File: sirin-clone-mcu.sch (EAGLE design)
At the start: 3 parts, among them J1 PJ-002A

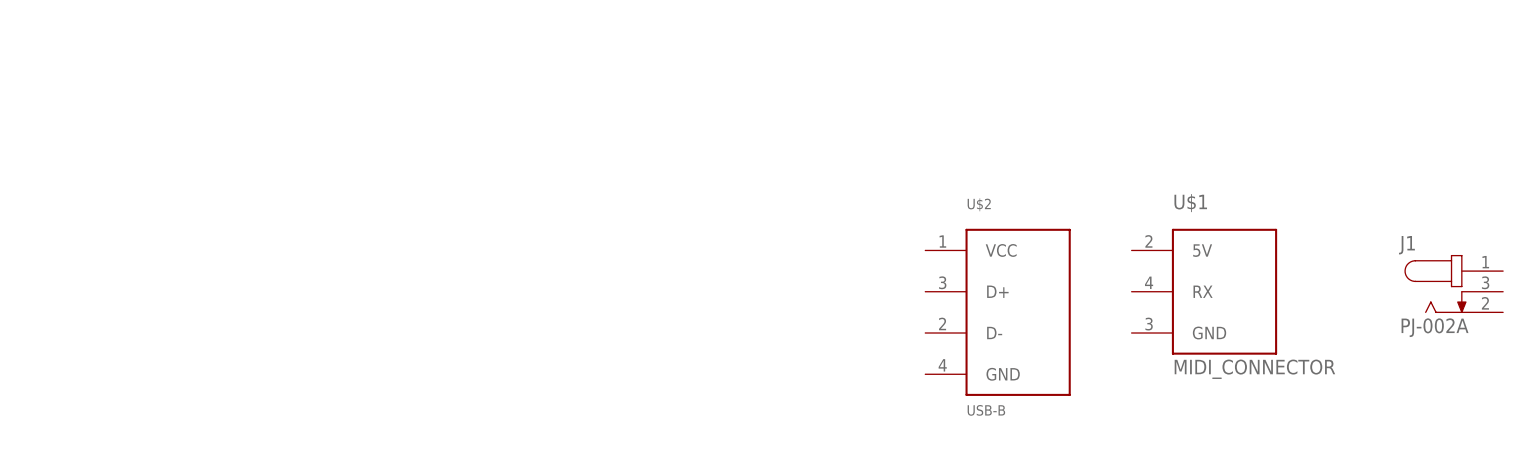
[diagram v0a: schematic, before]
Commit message: add midi
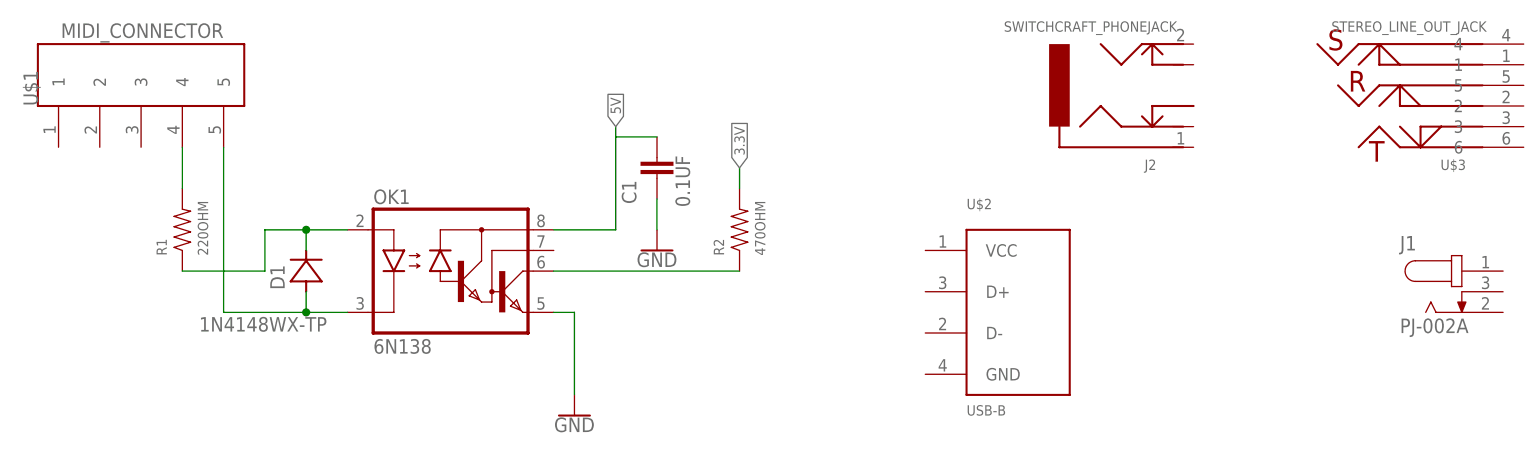
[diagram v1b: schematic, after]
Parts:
- added C1: 0.1UF, sirin-clone-library:0.1UF
- added D1: 1N4148WX-TP, sirin-clone-library:1N4148WX-TP
- added J2: SWITCHCRAFT_PHONEJACK, sirin-clone-library:SWITCHCRAFT_PHONEJACK
- added OK1: 6N138, sirin-clone-library:6N138
- added R1: 220OHM, sirin-clone-library:220OHM
- added R2: 470OHM, sirin-clone-library:470OHM
- added U$3: STEREO_LINE_OUT_JACK, sirin-clone-library:STEREO_LINE_OUT_JACK
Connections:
- new net 3.3V: R2.2
- new net 5V: C1.+, OK1.VCC
- new net GND: C1.-, OK1.GND
- new net N$1: D1.A, OK1.C, U$1.5
- new net N$2: R1.2, U$1.4
- new net N$3: D1.C, OK1.A, R1.1
- new net N$4: OK1.VO, R2.1
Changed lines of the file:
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@@
 </classes>
 <parts>
-<part name="U$1" library="sirin-clone-library" library_urn="urn:adsk.eagle:library:9336050" deviceset="MIDI_CONNECTOR" device="" package3d_urn="urn:adsk.eagle:package:9699785/3"/>
 <part name="J1" library="sirin-clone-library" library_urn="urn:adsk.eagle:library:9336050" deviceset="PJ-002A" device="" package3d_urn="urn:adsk.eagle:package:9702177/2"/>
 <part name="U$2" library="sirin-clone-library" library_urn="urn:adsk.eagle:library:9336050" deviceset="USB-B" device="" package3d_urn="urn:adsk.eagle:package:9702591/4"/>
+<part name="J2" library="sirin-clone-library" library_urn="urn:adsk.eagle:library:9336050" deviceset="SWITCHCRAFT_PHONEJACK" device="" package3d_urn="urn:adsk.eagle:package:8442329/2"/>
+<part name="U$3" library="sirin-clone-library" library_urn="urn:adsk.eagle:library:9336050" deviceset="STEREO_LINE_OUT_JACK" device="" package3d_urn="urn:adsk.eagle:package:9702873/3"/>
+<part name="D1" library="sirin-clone-library" library_urn="urn:adsk.eagle:library:9336050" deviceset="1N4148WX-TP" device="" package3d_urn="urn:adsk.eagle:package:9797239/2"/>
+<part name="R1" library="sirin-clone-library" library_urn="urn:adsk.eagle:library:9336050" deviceset="220OHM" device="" package3d_urn="urn:adsk.eagle:package:8442354/2"/>
+<part name="C1" library="sirin-clone-library" library_urn="urn:adsk.eagle:library:9336050" deviceset="0.1UF" device="" package3d_urn="urn:adsk.eagle:package:8442351/2"/>
+<part name="R2" library="sirin-clone-library" library_urn="urn:adsk.eagle:library:9336050" deviceset="470OHM" device="" package3d_urn="urn:adsk.eagle:package:8442354/2"/>
+<part name="U$1" library="sirin-clone-library" library_urn="urn:adsk.eagle:library:9336050" deviceset="MIDI_CONNECTOR" device="" package3d_urn="urn:adsk.eagle:package:9699785/3"/>
+<part name="OK1" library="sirin-clone-library" library_urn="urn:adsk.eagle:library:9336050" deviceset="6N138" device="" package3d_urn="urn:adsk.eagle:package:9797260/1"/>
+<part name="GND1" library="sirin-clone-library" library_urn="urn:adsk.eagle:library:9336050" deviceset="GND" device=""/>
+<part name="GND2" library="sirin-clone-library" library_urn="urn:adsk.eagle:library:9336050" deviceset="GND" device=""/>
 </parts>
 <sheets>
@@
 </plain>
 <instances>
-<instance part="U$1" gate="G$1" x="20.32" y="38.1" smashed="yes">
-<attribute name="NAME" x="15.24" y="48.26" size="1.778" layer="95"/>
-<attribute name="VALUE" x="15.24" y="27.94" size="1.778" layer="96"/>
-</instance>
 <instance part="J1" gate="G$1" x="50.8" y="38.1" smashed="yes">
 <attribute name="NAME" x="43.17881875" y="43.180790625" size="1.77828125" layer="95"/>
@@
 <attribute name="VALUE" x="-10.16" y="22.86" size="1.27" layer="96"/>
 </instance>
+<instance part="J2" gate="J1" x="10.16" y="63.5" smashed="yes">
+<attribute name="VALUE" x="15.748" y="71.374" size="1.27" layer="96" rot="R180"/>
+<attribute name="NAME" x="13.208" y="54.356" size="1.27" layer="95" rot="R180"/>
+</instance>
+<instance part="U$3" gate="G$1" x="48.26" y="63.5" smashed="yes">
+<attribute name="VALUE" x="53.848" y="71.374" size="1.27" layer="96" rot="R180"/>
+<attribute name="NAME" x="51.308" y="54.356" size="1.27" layer="95" rot="R180"/>
+</instance>
+<instance part="D1" gate="D1" x="-91.44" y="40.64" smashed="yes" rot="R90">
+<attribute name="NAME" x="-94.0816" y="38.3286" size="1.778" layer="95" rot="R90"/>
+<attribute name="VALUE" x="-88.8746" y="34.9758" size="1.778" layer="96" rot="R180"/>
+</instance>
+<instance part="R1" gate="R1" x="-106.68" y="45.72" smashed="yes" rot="R90">
+<attribute name="NAME" x="-108.585" y="42.545" size="1.27" layer="95" rot="R90"/>
+<attribute name="VALUE" x="-103.505" y="42.545" size="1.27" layer="96" rot="R90"/>
+</instance>
+<instance part="C1" gate="C1" x="-48.26" y="53.34" smashed="yes">
+<attribute name="VALUE" x="-44.196" y="48.514" size="1.778" layer="96" font="vector" rot="R90"/>
+<attribute name="NAME" x="-50.8" y="48.895" size="1.778" layer="95" rot="R90"/>
+</instance>
+<instance part="R2" gate="R1" x="-38.1" y="45.72" smashed="yes" rot="R90">
+<attribute name="NAME" x="-40.005" y="42.545" size="1.27" layer="95" rot="R90"/>
+<attribute name="VALUE" x="-34.925" y="42.545" size="1.27" layer="96" rot="R90"/>
+</instance>
+<instance part="U$1" gate="G$1" x="-111.76" y="66.04" smashed="yes" rot="R90">
+<attribute name="NAME" x="-124.46" y="60.96" size="1.778" layer="95" rot="R90"/>
+<attribute name="VALUE" x="-101.6" y="71.12" size="1.778" layer="96" rot="R180"/>
+</instance>
+<instance part="OK1" gate="G$1" x="-73.66" y="40.64" smashed="yes">
+<attribute name="NAME" x="-83.185" y="48.895" size="1.778" layer="95"/>
+<attribute name="VALUE" x="-83.185" y="30.48" size="1.778" layer="96"/>
+</instance>
+<instance part="GND1" gate="1" x="-58.42" y="22.86" smashed="yes">
+<attribute name="VALUE" x="-58.42" y="22.606" size="1.778" layer="96" align="top-center"/>
+</instance>
+<instance part="GND2" gate="1" x="-48.26" y="43.18" smashed="yes">
+<attribute name="VALUE" x="-48.26" y="42.926" size="1.778" layer="96" align="top-center"/>
+</instance>
 </instances>
 <busses>
 </busses>
 <nets>
+<net name="N$1" class="0">
+<segment>
+<pinref part="U$1" gate="G$1" pin="5"/>
+<wire x1="-101.6" y1="55.88" x2="-101.6" y2="35.56" width="0.1524" layer="91"/>
+<pinref part="OK1" gate="G$1" pin="C"/>
+<wire x1="-101.6" y1="35.56" x2="-91.44" y2="35.56" width="0.1524" layer="91"/>
+<pinref part="D1" gate="D1" pin="A"/>
+<wire x1="-91.44" y1="35.56" x2="-86.36" y2="35.56" width="0.1524" layer="91"/>
+<wire x1="-91.44" y1="38.1" x2="-91.44" y2="35.56" width="0.1524" layer="91"/>
+<junction x="-91.44" y="35.56"/>
+</segment>
+</net>
+<net name="N$2" class="0">
+<segment>
+<pinref part="R1" gate="R1" pin="2"/>
+<pinref part="U$1" gate="G$1" pin="4"/>
+<wire x1="-106.68" y1="50.8" x2="-106.68" y2="55.88" width="0.1524" layer="91"/>
+</segment>
+</net>
+<net name="N$3" class="0">
+<segment>
+<pinref part="R1" gate="R1" pin="1"/>
+<wire x1="-106.68" y1="40.64" x2="-96.52" y2="40.64" width="0.1524" layer="91"/>
+<wire x1="-96.52" y1="40.64" x2="-96.52" y2="45.72" width="0.1524" layer="91"/>
+<pinref part="OK1" gate="G$1" pin="A"/>
+<wire x1="-96.52" y1="45.72" x2="-91.44" y2="45.72" width="0.1524" layer="91"/>
+<pinref part="D1" gate="D1" pin="C"/>
+<wire x1="-91.44" y1="45.72" x2="-86.36" y2="45.72" width="0.1524" layer="91"/>
+<wire x1="-91.44" y1="43.18" x2="-91.44" y2="45.72" width="0.1524" layer="91"/>
+<junction x="-91.44" y="45.72"/>
+</segment>
+</net>
+<net name="5V" class="0">
+<segment>
+<pinref part="OK1" gate="G$1" pin="VCC"/>
+<wire x1="-60.96" y1="45.72" x2="-53.34" y2="45.72" width="0.1524" layer="91"/>
+<wire x1="-53.34" y1="45.72" x2="-53.34" y2="57.15" width="0.1524" layer="91"/>
+<label x="-53.34" y="58.42" size="1.27" layer="95" rot="R90" xref="yes"/>
+<pinref part="C1" gate="C1" pin="+"/>
+<wire x1="-48.26" y1="57.15" x2="-53.34" y2="57.15" width="0.1524" layer="91"/>
+<wire x1="-53.34" y1="57.15" x2="-53.34" y2="58.42" width="0.1524" layer="91"/>
+</segment>
+</net>
+<net name="GND" class="0">
+<segment>
+<pinref part="OK1" gate="G$1" pin="GND"/>
+<wire x1="-60.96" y1="35.56" x2="-58.42" y2="35.56" width="0.1524" layer="91"/>
+<pinref part="GND1" gate="1" pin="GND"/>
+<wire x1="-58.42" y1="35.56" x2="-58.42" y2="25.4" width="0.1524" layer="91"/>
+</segment>
+<segment>
+<pinref part="GND2" gate="1" pin="GND"/>
+<wire x1="-48.26" y1="45.72" x2="-48.26" y2="49.53" width="0.1524" layer="91"/>
+<pinref part="C1" gate="C1" pin="-"/>
+</segment>
+</net>
+<net name="N$4" class="0">
+<segment>
+<pinref part="OK1" gate="G$1" pin="VO"/>
+<pinref part="R2" gate="R1" pin="1"/>
+<wire x1="-60.96" y1="40.64" x2="-38.1" y2="40.64" width="0.1524" layer="91"/>
+</segment>
+</net>
+<net name="3.3V" class="0">
+<segment>
+<pinref part="R2" gate="R1" pin="2"/>
+<wire x1="-38.1" y1="50.8" x2="-38.1" y2="53.34" width="0.1524" layer="91"/>
+<label x="-38.1" y="53.34" size="1.27" layer="95" rot="R90" xref="yes"/>
+</segment>
+</net>
 </nets>
 </sheet>

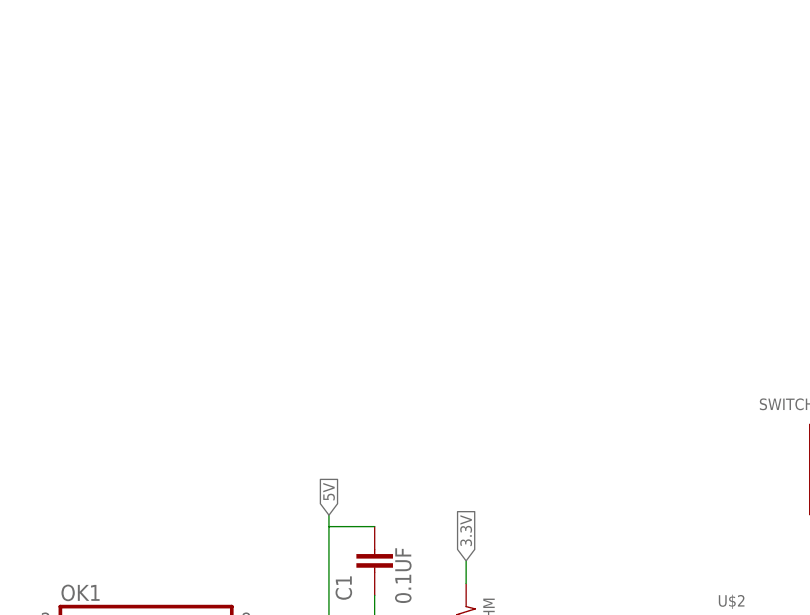
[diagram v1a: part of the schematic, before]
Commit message: work on connector options
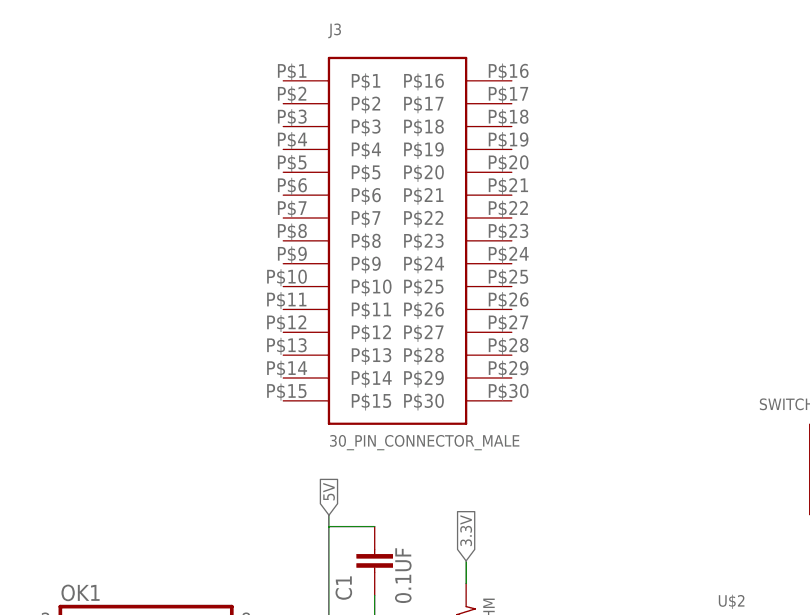
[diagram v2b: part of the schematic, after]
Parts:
- added J3: 30_PIN_CONNECTOR_MALE, sirin-clone-library:30_PIN_CONNECTOR_MALE
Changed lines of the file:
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@@
 <?xml version="1.0" encoding="utf-8"?>
 <!DOCTYPE eagle SYSTEM "eagle.dtd">
-<eagle version="9.3.0">
+<eagle version="9.3.1">
 <drawing>
 <settings>
@@
 <part name="GND1" library="sirin-clone-library" library_urn="urn:adsk.eagle:library:9336050" deviceset="GND" device=""/>
 <part name="GND2" library="sirin-clone-library" library_urn="urn:adsk.eagle:library:9336050" deviceset="GND" device=""/>
+<part name="J3" library="sirin-clone-library" library_urn="urn:adsk.eagle:library:9336050" deviceset="30_PIN_CONNECTOR_MALE" device="" package3d_urn="urn:adsk.eagle:package:9858341/2"/>
 </parts>
 <sheets>
@@
 <attribute name="VALUE" x="-48.26" y="42.926" size="1.778" layer="96" align="top-center"/>
 </instance>
+<instance part="J3" gate="J1" x="-45.72" y="88.9" smashed="yes">
+<attribute name="NAME" x="-53.34" y="111.76" size="1.27" layer="95"/>
+<attribute name="VALUE" x="-53.34" y="66.04" size="1.27" layer="96"/>
+</instance>
 </instances>

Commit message: routing
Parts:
- removed J2: SWITCHCRAFT_PHONEJACK, sirin-clone-library:SWITCHCRAFT_PHONEJACK
- added C10, C14, C27, C28, C29, C3, C35, C8, C9: 0.1UF, moon-germs-v1_main:0.1UF
- added C11, C12: 22PF, moon-germs-v1_main:22PF
- added C13, C26, C33, C34, C4, C7: 2.2UF, moon-germs-v1_main:2.2UF
- added C31, C32: 1.0UF, moon-germs-v1_main:1.0UF
- added C36: 0.15UF, moon-germs-v1_main:0.15UF
- added D5: ORANGE, moon-germs-v1_main:LED_ORANGE0805
- added D6: AP7313, moon-germs-v1:AP7313
- added FUSE2: (no value), moon-germs-v1_main:FUSE
- added G3: 16MHz, moon-germs-v1_main:CRYSTAL-HC49US
- added G4: 32.768kHz, moon-germs-v1_main:CRYSTAL-TC26H
- added J5: SWITCHCRAFT_PHONEJACK, moon-germs-v1_main:SWITCHCRAFT_PHONEJACK
- added J6: SWD_CONNECTOR, moon-germs-v1_main:SWD_CONNECTOR
- added K3: (no value), moon-germs-v1_main:MK20DX256VLH7
- added K4: (no value), moon-germs-v1_main:MKL04Z32VLC4
- added L1, L4: (no value), moon-germs-v1_main:FERRITE600_TEENSY
- added L3: FERRITE600, moon-germs-v1_main:FERRITE600
- added R11, R12: 2.2K, moon-germs-v1_main:2.2KOHM
- added R13, R14: 10K, moon-germs-v1_main:10KOHM
- added R17: 1K, moon-germs-v1_main:1KOHM
- added R18: 100K, moon-germs-v1_main:100KOHM
- added R5, R6: 33, moon-germs-v1_main:33OHM
- added R7, R8: 470, moon-germs-v1_main:470OHM
- added S2: (no value), moon-germs-v1_main:TACT_SWITCH
- added T2: MCP1825S, moon-germs-v1_main:LDO
- added U$6: MICROSD, moon-germs-v1_main:MICROSD
- added U4: SGTL5000_32QFN, moon-germs-v1_main:SGTL5000_32QFN
- added U5: 23LC1024, moon-germs-v1_main:23LC1024
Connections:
- removed net 5V: C1.+, OK1.VCC
- new net AGND: C13.-, C14.-, C27.-, K3.VREFL, K3.VSSA, L4.2
- new net AMPSD: J5.TIPSWITCH(4), R18.2
- new net AREF: C14.+, K3.VREFH, R8.2
- new net D+: R6.1, U$2.D+
- new net D-: R5.1, U$2.D-
- new net EN': J6.EN', K4.PTA3
- new net N$10: G4.2, K3.EXTAL32
- new net N$11: G4.1, K3.XTAL32
- new net N$12: C12.+, G3.2, K3.PTA19
- new net N$13: C11.+, G3.1, K3.PTA18
- new net N$14: C13.+, K3.VDDA, L1.1, R8.1
- new net N$15: C27.+, K3.VREF_OUT
- new net N$19: C36.+, U4.VAG(10)
- new net N$20: C33.+, D6.OUT, U4.VDDD(30)
- new net N$21: C34.+, C35.+, L3.2, U4.VDDA(5)
- new net N$8: K3.PTA2, K4.PTB1
- new net N$9: D5.C, R7.2
- new net PIN0/SW1: K3.PTB16
- new net PIN1/SW2: K3.PTB17
- new net PIN10/DAT3: K3.PTC4, R14.1, U$6.DAT3(CS,2)
- new net PIN11/MCLK: K3.PTC6, U4.MCLK(21)
- new net PIN12/DAT0: K3.PTC7, U$6.DAT0(D0,7), U5.MISO(2)
- new net PIN13/RX: D5.A, K3.PTC5, U4.RX(25)
- new net PIN14/CLK: K3.PTD1, U$6.CLK(SCLK,5), U5.SCLK(6)
- new net PIN15(VOL): K3.PTC0
- new net PIN16: K3.PTB0
- new net PIN17: K3.PTB1
- new net PIN18/SDA: K3.PTB3, R12.1, U4.SDA(27)
- new net PIN19/SCL: K3.PTB2, R11.1, U4.SCL(29)
- new net PIN2: K3.PTD0
- new net PIN20/ENC_LED_G: K3.PTD5
- new net PIN21/ENC_LED_R: K3.PTD6
- new net PIN22/TX: K3.PTC1, U4.TX(26)
- new net PIN23/LRCLK: K3.PTC2, U4.LRCLK(23)
- new net PIN24: K3.PTA5
- new net PIN25: K3.PTB19
- new net PIN26: K3.PTE1
- new net PIN27: K3.PTC9
- new net PIN28: K3.PTC8
- new net PIN29: K3.PTC10
- new net PIN3: K3.PTA12
- new net PIN30: K3.PTC11
- new net PIN31: K3.PTE0
- new net PIN32/SW3: K3.PTB18
- new net PIN33: K3.PTA4
- new net PIN4/ENCA: K3.PTA13
- new net PIN5/ENCB: K3.PTD7
- new net PIN6/CS: K3.PTD4, R13.2, U5.CS(1)
- new net PIN7/CMD: K3.PTD2, U$6.CMD(DI,3), U5.MOSI(5)
- new net PIN8/ENCSW: K3.PTD3
- new net PIN9/BCLK: K3.PTC3, U4.BCLK(24)
- new net PINA10: K3.ADC0_DP0
- new net PINA11: K3.ADC0_DM0
- new net PINA12: K3.ADC0_DP3
- new net PINA13: K3.ADC0_DM3
- new net PINA14/MOD: K3.DAC0
- new net PROG: K4.PTB2, S2.1
- new net RING/R: J5.RING(3), U4.HPR(2)
- new net RST: J6.RESET, K3.RESET_B, K4.PTA4, K4.PTB5
- new net SLEEVE: J5.SLEEVE(1), U4.HPVGND(4)
- new net SWC: J6.SWC, K3.PTA0, K4.PTB0
- new net SWD: J6.SWD, K3.PTA3, K4.PTA7
- new net TIP/L: J5.TIP(2), R17.1, U4.HPL(6)
- new net USB_DM: K3.USB0_DM, R5.2
- new net USB_DP: K3.USB0_DP, R6.2
- new net USB_ID: K3.PTA1, K4.PTA6
- new net VIN_5V: C3.+, J1.1, T2.IN
- new net VUSB: FUSE2.2
- new net VUSB_IN: C4.+, FUSE2.1, U$2.VCC
- net 3.3V: now also C1.+, C10.+, C26.+, C28.+, C29.+, C31.+, C32.+, C7.+, C8.+, C9.+, D6.IN, K3.VBAT, K3.VDD@3, K3.VDD@30, K3.VDD@48, K3.VOUT33, K4.VDD, K4.VREFH, L1.2, L3.1, OK1.VCC, R11.2, R12.2, R13.1, R14.2, R17.2, T2.OUT, U$6.VDD(4), U4.VDDIO(20), U5.3.3V(8), U5.RST(7), U5.WP(3)
- net GND: now also C10.-, C11.-, C12.-, C26.-, C28.-, C29.-, C3.-, C31.-, C32.-, C33.-, C34.-, C35.-, C36.-, C4.-, C7.-, C8.-, C9.-, D6.GND, J1.2, J6.GND, K3.VSS@31, K3.VSS@4, K3.VSS@47, K4.VREFL, K4.VSS, L4.1, R18.1, R7.1, S2.3, T2.GND, T2.PAD, U$2.GND, U$6.VSS(6), U4.ADDR(31), U4.AGND(7), U4.GND@1, U4.GND@3, U4.GND@PAD, U4.MODE(32), U5.GND(4)
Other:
- moved on the sheet: J1, U$2, U$3

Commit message: more routing
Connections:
- net PIN0/SW1 renamed PIN0/MIDIIN
- net PIN1/SW2 renamed PIN1/MIDIOUT
- removed net PIN15(VOL): K3.PTC0
- removed net PIN16: K3.PTB0
- removed net PIN17: K3.PTB1
- removed net PIN2: K3.PTD0
- removed net PIN20/ENC_LED_G: K3.PTD5
- removed net PIN21/ENC_LED_R: K3.PTD6
- removed net PIN24: K3.PTA5
- removed net PIN25: K3.PTB19
- removed net PIN26: K3.PTE1
- removed net PIN27: K3.PTC9
- removed net PIN28: K3.PTC8
- removed net PIN29: K3.PTC10
- removed net PIN3: K3.PTA12
- removed net PIN30: K3.PTC11
- removed net PIN31: K3.PTE0
- removed net PIN32/SW3: K3.PTB18
- removed net PIN33: K3.PTA4
- removed net PIN4/ENCA: K3.PTA13
- removed net PIN5/ENCB: K3.PTD7
- removed net PIN8/ENCSW: K3.PTD3
- removed net PINA10: K3.ADC0_DP0
- removed net PINA11: K3.ADC0_DM0
- removed net PINA12: K3.ADC0_DP3
- removed net PINA13: K3.ADC0_DM3
- removed net PINA14/MOD: K3.DAC0
- new net PIN15/KNOB1(VOL): J3.P$5, K3.PTC0
- new net PIN16/KNOB2: J3.P$6, K3.PTB0
- new net PIN17/KNOB3: J3.P$7, K3.PTB1
- new net PIN2/SW1: J3.P$1, K3.PTD0
- new net PIN20/KNOB4: J3.P$8, K3.PTD5
- new net PIN21/KNOB5: J3.P$9, K3.PTD6
- new net PIN24/LED1: J3.P$22, K3.PTA5
- new net PIN25/LED2: J3.P$23, K3.PTB19
- new net PIN26/KNOB6: J3.P$10, K3.PTE1
- new net PIN27/KNOB7: J3.P$11, K3.PTC9
- new net PIN28/KNOB8: J3.P$12, K3.PTC8
- new net PIN29/KNOB9: J3.P$13, K3.PTC10
- new net PIN3/SW2: J3.P$2, K3.PTA12
- new net PIN30/KNOB10: J3.P$14, K3.PTC11
- new net PIN31/KNOB11: J3.P$15, K3.PTE0
- new net PIN32/LED3: J3.P$24, K3.PTB18
- new net PIN33/LED4: J3.P$25, K3.PTA4
- new net PIN4/SW3: J3.P$3, K3.PTA13
- new net PIN5/SW4: J3.P$4, K3.PTD7
- new net PIN8/MIDILED: J3.P$21, K3.PTD3
- new net PINA10/KNOB12: J3.P$16, K3.ADC0_DP0
- new net PINA11/KNOB13: J3.P$17, K3.ADC0_DM0
- new net PINA12/KNOB14: J3.P$18, K3.ADC0_DP3
- new net PINA13/KNOB15: J3.P$19, K3.ADC0_DM3
- new net PINA14/KNOB16: J3.P$20, K3.DAC0
- net 3.3V: now also J3.P$26, J3.P$27, J3.P$28
- net GND: now also J3.P$29, J3.P$30
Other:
- moved on the sheet: D5, J3, R7

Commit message: lots o' routing
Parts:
- removed R17: 1K, moon-germs-v1_main:1KOHM
- removed R18: 100K, moon-germs-v1_main:100KOHM
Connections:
- removed net AMPSD: J5.TIPSWITCH(4), R18.2
- new net N$27: J3.P$2
- net 3.3V: now also J3.P$14, J3.P$15; no longer J3.P$26, J3.P$27, J3.P$28, R17.2
- net GND: no longer R18.1
- net PIN15/KNOB1(VOL): now also J3.P$24; no longer J3.P$5
- net PIN16/KNOB2: now also J3.P$28; no longer J3.P$6
- net PIN17/KNOB3: now also J3.P$27; no longer J3.P$7
- net PIN2/SW1: now also J3.P$19; no longer J3.P$1
- net PIN20/KNOB4: now also J3.P$4; no longer J3.P$8
- net PIN21/KNOB5: now also J3.P$5; no longer J3.P$9
- net PIN24/LED1: now also J3.P$16; no longer J3.P$22
- net PIN25/LED2: now also J3.P$25; no longer J3.P$23
- net PIN26/KNOB6: now also J3.P$9; no longer J3.P$10
- net PIN27/KNOB7: now also J3.P$22; no longer J3.P$11
- net PIN28/KNOB8: now also J3.P$23; no longer J3.P$12
- net PIN29/KNOB9: now also J3.P$21; no longer J3.P$13
- net PIN3/SW2: now also J3.P$17; no longer J3.P$2
- net PIN30/KNOB10: now also J3.P$20; no longer J3.P$14
- net PIN31/KNOB11: now also J3.P$8; no longer J3.P$15
- net PIN32/LED3: now also J3.P$26; no longer J3.P$24
- net PIN33/LED4: now also J3.P$1; no longer J3.P$25
- net PIN4/SW3: now also J3.P$18; no longer J3.P$3
- net PIN5/SW4: now also J3.P$6; no longer J3.P$4
- net PIN8/MIDILED: now also J3.P$3; no longer J3.P$21
- net PINA10/KNOB12: now also J3.P$11; no longer J3.P$16
- net PINA11/KNOB13: now also J3.P$10; no longer J3.P$17
- net PINA12/KNOB14: now also J3.P$12; no longer J3.P$18
- net PINA13/KNOB15: now also J3.P$13; no longer J3.P$19
- net PINA14/KNOB16: now also J3.P$7; no longer J3.P$20
- net TIP/L: no longer R17.1
- net VUSB: now also U$2.VCC
- net VUSB_IN: no longer U$2.VCC
